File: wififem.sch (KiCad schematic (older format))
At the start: 36 parts, among them J1 Conn_Coaxial, J2 Conn_Coaxial, J3 Conn_Coaxial, J4 Conn_Coaxial, U1 MCP6566, U2 74HCT04, U3 SE2611T

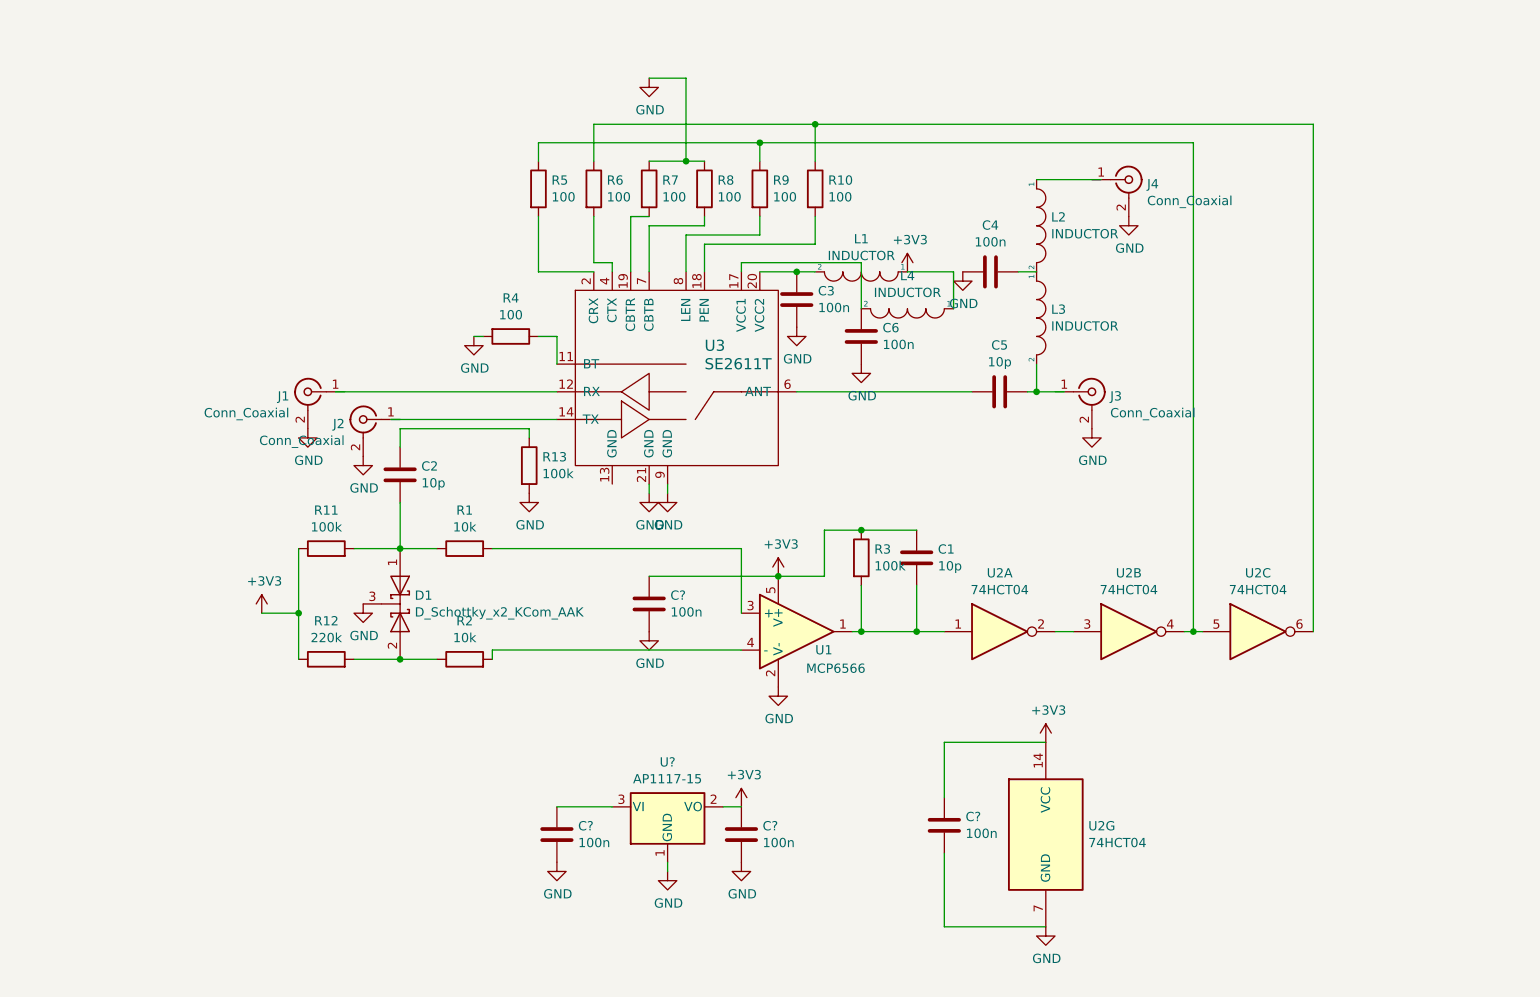
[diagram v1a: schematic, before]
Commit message: Replaced directional coupler with simple parallel connection. Layout almost done
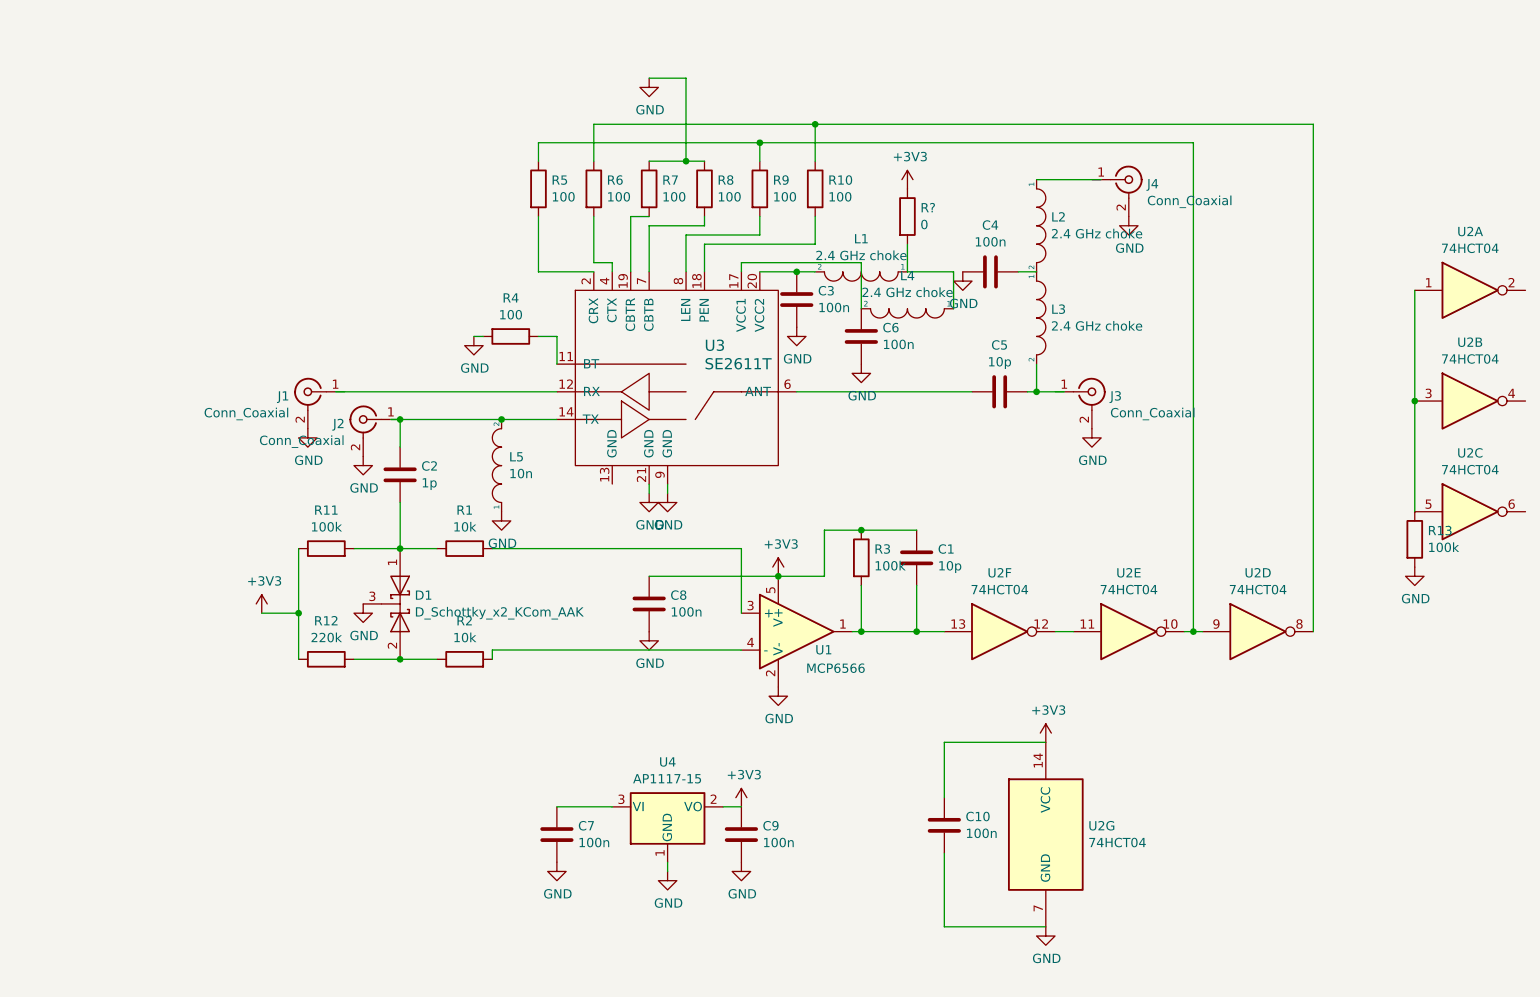
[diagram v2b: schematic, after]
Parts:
- added L5: 10n, Inductors_SMD:L_0805_HandSoldering, symbol pspice:INDUCTOR
- added R?: 0, Resistors_SMD:R_0805_HandSoldering, symbol device:R
- added unit 4 of U2
- added unit 5 of U2
- added unit 6 of U2
- C2: value 10p -> 1p
- L1, L2, L3, L4: value INDUCTOR -> 2.4 GHz choke
- gave numbers to parts that had none: 5
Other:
- moved on the sheet: U2A, U2B, U2C
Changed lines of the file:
@@
 L Logic_74xx:74HCT04 U2
 U 1 1 5A159D7B
-P 7400 3950
-F 0 "U2" H 7400 4267 50  0000 C CNN
-F 1 "74HCT04" H 7400 4176 50  0000 C CNN
-F 2 "Housings_SOIC:SOIC-14_3.9x8.7mm_Pitch1.27mm" H 7400 3950 50  0001 C CNN
-F 3 "http://www.nxp.com/documents/data_sheet/74HC_HCT04.pdf" H 7400 3950 50  0001 C CNN
-	1    7400 3950
+P 9950 2100
+F 0 "U2" H 9950 2417 50  0000 C CNN
+F 1 "74HCT04" H 9950 2326 50  0000 C CNN
+F 2 "Housings_SOIC:SOIC-14_3.9x8.7mm_Pitch1.27mm" H 9950 2100 50  0001 C CNN
+F 3 "http://www.nxp.com/documents/data_sheet/74HC_HCT04.pdf" H 9950 2100 50  0001 C CNN
+	1    9950 2100
 	1    0    0    -1
 $EndComp
@@
 L Logic_74xx:74HCT04 U2
 U 2 1 5A159F5E
-P 8100 3950
-F 0 "U2" H 8100 4267 50  0000 C CNN
-F 1 "74HCT04" H 8100 4176 50  0000 C CNN
-F 2 "" H 8100 3950 50  0001 C CNN
-F 3 "http://www.nxp.com/documents/data_sheet/74HC_HCT04.pdf" H 8100 3950 50  0001 C CNN
-	2    8100 3950
-	1    0    0    -1
-$EndComp
-$Comp
-L Logic_74xx:74HCT04 U2
-U 3 1 5A15A004
-P 8800 3950
-F 0 "U2" H 8800 4267 50  0000 C CNN
-F 1 "74HCT04" H 8800 4176 50  0000 C CNN
-F 2 "" H 8800 3950 50  0001 C CNN
-F 3 "http://www.nxp.com/documents/data_sheet/74HC_HCT04.pdf" H 8800 3950 50  0001 C CNN
-	3    8800 3950
+P 9950 2700
+F 0 "U2" H 9950 3017 50  0000 C CNN
+F 1 "74HCT04" H 9950 2926 50  0000 C CNN
+F 2 "" H 9950 2700 50  0001 C CNN
+F 3 "http://www.nxp.com/documents/data_sheet/74HC_HCT04.pdf" H 9950 2700 50  0001 C CNN
+	2    9950 2700
 	1    0    0    -1
 $EndComp
@@
 P 7600 2250
 F 0 "L3" V 7554 2328 50  0000 L CNN
-F 1 "INDUCTOR" V 7645 2328 50  0000 L CNN
+F 1 "2.4 GHz choke" V 7645 2328 50  0000 L CNN
 F 2 "Inductors_SMD:L_0805_HandSoldering" H 7600 2250 50  0001 C CNN
 F 3 "" H 7600 2250 50  0001 C CNN
@@
 P 4150 3100
 F 0 "C2" H 4035 3054 50  0000 R CNN
-F 1 "10p" H 4035 3145 50  0000 R CNN
+F 1 "1p" H 4035 3145 50  0000 R CNN
 F 2 "Capacitors_SMD:C_0805_HandSoldering" H 4188 2950 50  0001 C CNN
 F 3 "" H 4150 3100 50  0001 C CNN
@@
 P 7600 1750
 F 0 "L2" V 7554 1828 50  0000 L CNN
-F 1 "INDUCTOR" V 7645 1828 50  0000 L CNN
+F 1 "2.4 GHz choke" V 7645 1828 50  0000 L CNN
 F 2 "Inductors_SMD:L_0805_HandSoldering" H 7600 1750 50  0001 C CNN
 F 3 "" H 7600 1750 50  0001 C CNN
@@
 P 6650 2000
 F 0 "L1" H 6650 1822 50  0000 C CNN
-F 1 "INDUCTOR" H 6650 1913 50  0000 C CNN
+F 1 "2.4 GHz choke" H 6650 1913 50  0000 C CNN
 F 2 "Inductors_SMD:L_0805_HandSoldering" H 6650 2000 50  0001 C CNN
 F 3 "" H 6650 2000 50  0001 C CNN
@@
 L power:+3V3 #PWR015
 U 1 1 5A17CF72
-P 6900 2000
-F 0 "#PWR015" H 6900 1850 50  0001 C CNN
-F 1 "+3V3" H 6915 2173 50  0000 C CNN
-F 2 "" H 6900 2000 50  0001 C CNN
-F 3 "" H 6900 2000 50  0001 C CNN
-	1    6900 2000
+P 6900 1550
+F 0 "#PWR015" H 6900 1400 50  0001 C CNN
+F 1 "+3V3" H 6915 1723 50  0000 C CNN
+F 2 "" H 6900 1550 50  0001 C CNN
+F 3 "" H 6900 1550 50  0001 C CNN
+	1    6900 1550
 	1    0    0    -1
 $EndComp
@@
 P 6900 2200
 F 0 "L4" H 6900 2022 50  0000 C CNN
-F 1 "INDUCTOR" H 6900 2113 50  0000 C CNN
+F 1 "2.4 GHz choke" H 6900 2113 50  0000 C CNN
 F 2 "Inductors_SMD:L_0805_HandSoldering" H 6900 2200 50  0001 C CNN
 F 3 "" H 6900 2200 50  0001 C CNN
@@
 	6000 1950 6000 2000
 Wire Wire Line
-	4150 2950 4150 2850
-Wire Wire Line
-	4150 2850 4850 2850
-Wire Wire Line
-	4850 2850 4850 2900
-$Comp
-L power:GND #PWR017
-U 1 1 5A18CCA2
-P 4850 3200
-F 0 "#PWR017" H 4850 2950 50  0001 C CNN
-F 1 "GND" H 4855 3027 50  0000 C CNN
-F 2 "" H 4850 3200 50  0001 C CNN
-F 3 "" H 4850 3200 50  0001 C CNN
-	1    4850 3200
-	1    0    0    -1
-$EndComp
+	4150 2800 4150 2950
 $Comp
 L device:D_Schottky_x2_KCom_AAK D1
@@
 	0    1    1    0
 $EndComp
-$Comp
-L device:R R13
-U 1 1 5A18D0FD
-P 4850 3050
-F 0 "R13" H 4920 3096 50  0000 L CNN
-F 1 "100k" H 4920 3005 50  0000 L CNN
-F 2 "Resistors_SMD:R_0805_HandSoldering" V 4780 3050 50  0001 C CNN
-F 3 "" H 4850 3050 50  0001 C CNN
-	1    4850 3050
-	1    0    0    -1
-$EndComp
 Wire Wire Line
 	4150 3250 4150 3500
@@
 Connection ~ 3600 3850
 $Comp
-L regul:AP1117-15 U?
+L regul:AP1117-15 U4
 U 1 1 5A1A47EC
 P 5600 4900
-F 0 "U?" H 5600 5142 50  0000 C CNN
+F 0 "U4" H 5600 5142 50  0000 C CNN
 F 1 "AP1117-15" H 5600 5051 50  0000 C CNN
 F 2 "TO_SOT_Packages_SMD:SOT-223-3_TabPin2" H 5600 5100 50  0001 C CNN
@@
 $EndComp
 $Comp
-L power:+3V3 #PWR?
+L power:+3V3 #PWR020
 U 1 1 5A1A48D5
 P 6000 4900
-F 0 "#PWR?" H 6000 4750 50  0001 C CNN
+F 0 "#PWR020" H 6000 4750 50  0001 C CNN
 F 1 "+3V3" H 6015 5073 50  0000 C CNN
 F 2 "" H 6000 4900 50  0001 C CNN
@@
 	6000 4900 5900 4900
 $Comp
-L power:GND #PWR?
+L power:GND #PWR021
 U 1 1 5A1A6D47
 P 5600 5250
-F 0 "#PWR?" H 5600 5000 50  0001 C CNN
+F 0 "#PWR021" H 5600 5000 50  0001 C CNN
 F 1 "GND" H 5605 5077 50  0000 C CNN
 F 2 "" H 5600 5250 50  0001 C CNN
@@
 	5600 5250 5600 5200
 $Comp
-L device:C C?
+L device:C C9
 U 1 1 5A1AA377
 P 6000 5050
-F 0 "C?" H 5885 5004 50  0000 R CNN
+F 0 "C9" H 5885 5004 50  0000 R CNN
 F 1 "100n" H 5885 5095 50  0000 R CNN
 F 2 "Capacitors_SMD:C_0805_HandSoldering" H 6038 4900 50  0001 C CNN
@@
 $EndComp
 $Comp
-L power:GND #PWR?
+L power:GND #PWR022
 U 1 1 5A1AA62D
 P 6000 5200
-F 0 "#PWR?" H 6000 4950 50  0001 C CNN
+F 0 "#PWR022" H 6000 4950 50  0001 C CNN
 F 1 "GND" H 6005 5027 50  0000 C CNN
 F 2 "" H 6000 5200 50  0001 C CNN
@@
 $EndComp
 $Comp
-L device:C C?
+L device:C C7
 U 1 1 5A1AA680
 P 5000 5050
-F 0 "C?" H 4885 5004 50  0000 R CNN
+F 0 "C7" H 4885 5004 50  0000 R CNN
 F 1 "100n" H 4885 5095 50  0000 R CNN
 F 2 "Capacitors_SMD:C_0805_HandSoldering" H 5038 4900 50  0001 C CNN
@@
 	5300 4900 5000 4900
 $Comp
-L power:GND #PWR?
+L power:GND #PWR023
 U 1 1 5A1ACCE4
 P 5000 5200
-F 0 "#PWR?" H 5000 4950 50  0001 C CNN
+F 0 "#PWR023" H 5000 4950 50  0001 C CNN
 F 1 "GND" H 5005 5027 50  0000 C CNN
 F 2 "" H 5000 5200 50  0001 C CNN
@@
 $EndComp
 $Comp
-L device:C C?
+L device:C C8
 U 1 1 5A1ACD39
 P 5500 3800
-F 0 "C?" H 5385 3754 50  0000 R CNN
+F 0 "C8" H 5385 3754 50  0000 R CNN
 F 1 "100n" H 5385 3845 50  0000 R CNN
 F 2 "Capacitors_SMD:C_0805_HandSoldering" H 5538 3650 50  0001 C CNN
@@
 Connection ~ 6200 3650
 $Comp
-L power:GND #PWR?
+L power:GND #PWR024
 U 1 1 5A1B10BA
 P 5500 3950
-F 0 "#PWR?" H 5500 3700 50  0001 C CNN
+F 0 "#PWR024" H 5500 3700 50  0001 C CNN
 F 1 "GND" H 5505 3777 50  0000 C CNN
 F 2 "" H 5500 3950 50  0001 C CNN
@@
 $EndComp
 $Comp
-L device:C C?
+L device:C C10
 U 1 1 5A1B1111
 P 7100 5000
-F 0 "C?" H 6985 4954 50  0000 R CNN
+F 0 "C10" H 6985 4954 50  0000 R CNN
 F 1 "100n" H 6985 5045 50  0000 R CNN
 F 2 "Capacitors_SMD:C_0805_HandSoldering" H 7138 4850 50  0001 C CNN
@@
 Wire Wire Line
 	7100 5550 7100 5150
+Connection ~ 4150 2800
+$Comp
+L pspice:INDUCTOR L5
+U 1 1 5A1BC783
+P 4700 3050
+F 0 "L5" V 4746 3010 50  0000 R CNN
+F 1 "10n" V 4655 3010 50  0000 R CNN
+F 2 "Inductors_SMD:L_0805_HandSoldering" H 4700 3050 50  0001 C CNN
+F 3 "" H 4700 3050 50  0001 C CNN
+	1    4700 3050
+	0    -1   -1   0
+$EndComp
+Connection ~ 4700 2800
+$Comp
+L power:GND #PWR017
+U 1 1 5A1C03BF
+P 4700 3300
+F 0 "#PWR017" H 4700 3050 50  0001 C CNN
+F 1 "GND" H 4705 3127 50  0000 C CNN
+F 2 "" H 4700 3300 50  0001 C CNN
+F 3 "" H 4700 3300 50  0001 C CNN
+	1    4700 3300
+	1    0    0    -1
+$EndComp
+$Comp
+L Logic_74xx:74HCT04 U2
+U 4 1 5A1C573B
+P 8800 3950
+F 0 "U2" H 8800 4267 50  0000 C CNN
+F 1 "74HCT04" H 8800 4176 50  0000 C CNN
+F 2 "" H 8800 3950 50  0001 C CNN
+F 3 "http://www.nxp.com/documents/data_sheet/74HC_HCT04.pdf" H 8800 3950 50  0001 C CNN
+	4    8800 3950
+	1    0    0    -1
+$EndComp
+$Comp
+L Logic_74xx:74HCT04 U2
+U 5 1 5A1C586C
+P 8100 3950
+F 0 "U2" H 8100 4267 50  0000 C CNN
+F 1 "74HCT04" H 8100 4176 50  0000 C CNN
+F 2 "" H 8100 3950 50  0001 C CNN
+F 3 "http://www.nxp.com/documents/data_sheet/74HC_HCT04.pdf" H 8100 3950 50  0001 C CNN
+	5    8100 3950
+	1    0    0    -1
+$EndComp
+$Comp
+L Logic_74xx:74HCT04 U2
+U 6 1 5A1C59B9
+P 7400 3950
+F 0 "U2" H 7400 4267 50  0000 C CNN
+F 1 "74HCT04" H 7400 4176 50  0000 C CNN
+F 2 "" H 7400 3950 50  0001 C CNN
+F 3 "http://www.nxp.com/documents/data_sheet/74HC_HCT04.pdf" H 7400 3950 50  0001 C CNN
+	6    7400 3950
+	1    0    0    -1
+$EndComp
+$Comp
+L Logic_74xx:74HCT04 U2
+U 3 1 5A15A004
+P 9950 3300
+F 0 "U2" H 9950 3617 50  0000 C CNN
+F 1 "74HCT04" H 9950 3526 50  0000 C CNN
+F 2 "" H 9950 3300 50  0001 C CNN
+F 3 "http://www.nxp.com/documents/data_sheet/74HC_HCT04.pdf" H 9950 3300 50  0001 C CNN
+	3    9950 3300
+	1    0    0    -1
+$EndComp
+Wire Wire Line
+	9650 2100 9650 3300
+Connection ~ 9650 2700
+$Comp
+L power:GND #PWR025
+U 1 1 5A1CD3BC
+P 9650 3600
+F 0 "#PWR025" H 9650 3350 50  0001 C CNN
+F 1 "GND" H 9655 3427 50  0000 C CNN
+F 2 "" H 9650 3600 50  0001 C CNN
+F 3 "" H 9650 3600 50  0001 C CNN
+	1    9650 3600
+	1    0    0    -1
+$EndComp
+$Comp
+L device:R R13
+U 1 1 5A1D64EB
+P 9650 3450
+F 0 "R13" H 9720 3496 50  0000 L CNN
+F 1 "100k" H 9720 3405 50  0000 L CNN
+F 2 "Resistors_SMD:R_0805_HandSoldering" V 9580 3450 50  0001 C CNN
+F 3 "" H 9650 3450 50  0001 C CNN
+	1    9650 3450
+	1    0    0    -1
+$EndComp
+$Comp
+L device:R R?
+U 1 1 5A1DB8B4
+P 6900 1700
+F 0 "R?" H 6970 1746 50  0000 L CNN
+F 1 "0" H 6970 1655 50  0000 L CNN
+F 2 "Resistors_SMD:R_0805_HandSoldering" V 6830 1700 50  0001 C CNN
+F 3 "" H 6900 1700 50  0001 C CNN
+	1    6900 1700
+	1    0    0    -1
+$EndComp
+Wire Wire Line
+	6900 1850 6900 2000
 $EndSCHEMATC

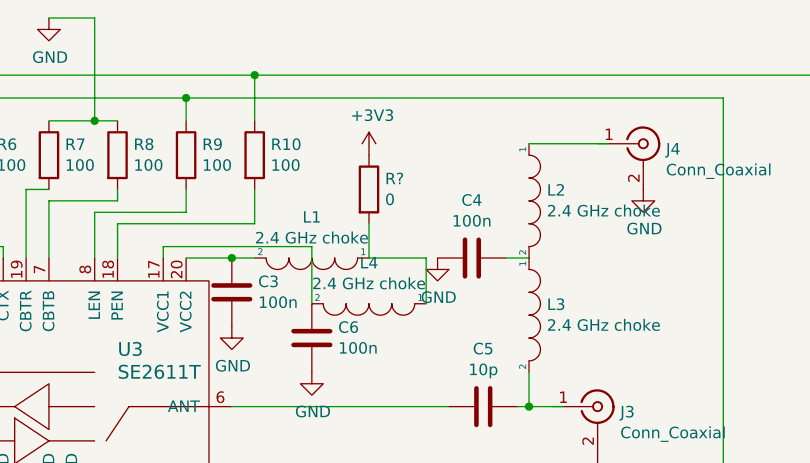
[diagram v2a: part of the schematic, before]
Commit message: RF layout improvement
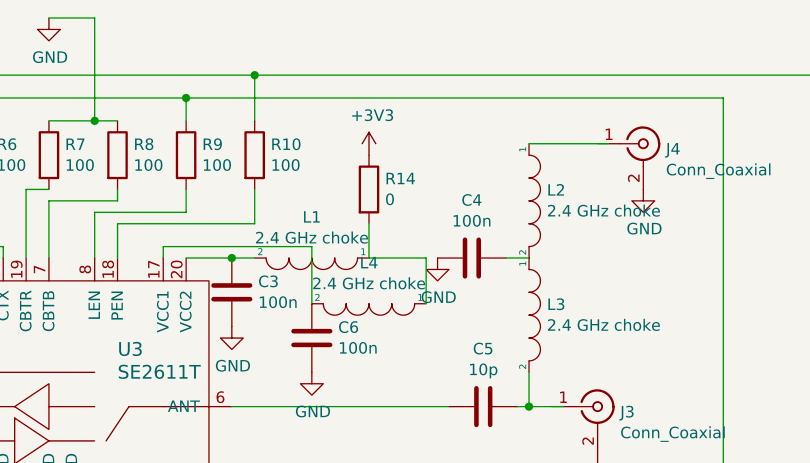
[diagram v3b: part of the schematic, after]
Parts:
- gave numbers to parts that had none: 1
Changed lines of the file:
@@
 $EndComp
 $Comp
-L device:R R?
+L device:R R14
 U 1 1 5A1DB8B4
 P 6900 1700
-F 0 "R?" H 6970 1746 50  0000 L CNN
+F 0 "R14" H 6970 1746 50  0000 L CNN
 F 1 "0" H 6970 1655 50  0000 L CNN
 F 2 "Resistors_SMD:R_0805_HandSoldering" V 6830 1700 50  0001 C CNN

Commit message: Everything in layout, DRC passes
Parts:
- removed J4: Conn_Coaxial, Connectors:SMA_THT_Jack_Straight, symbol Connector:Conn_Coaxial
- added D2: DIODE, Resistors_SMD:R_0805_HandSoldering, symbol pspice:DIODE
- added J4: Conn_01x05, Socket_Strips:Socket_Strip_Straight_1x05_Pitch2.54mm, symbol Connector:Conn_01x05
- added L6: ferrite bead, Inductors_SMD:L_0805_HandSoldering, symbol pspice:INDUCTOR
- added MK1, MK2, MK3, MK4: Mounting_Hole_PAD, Mounting_Holes:MountingHole_3.2mm_M3_Pad, symbol Mechanical:Mounting_Hole_PAD
- L1, L2, L4: value 2.4 GHz choke -> ferrite bead
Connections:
- wire segments 72 -> 84
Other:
- moved on the sheet: C4, L2

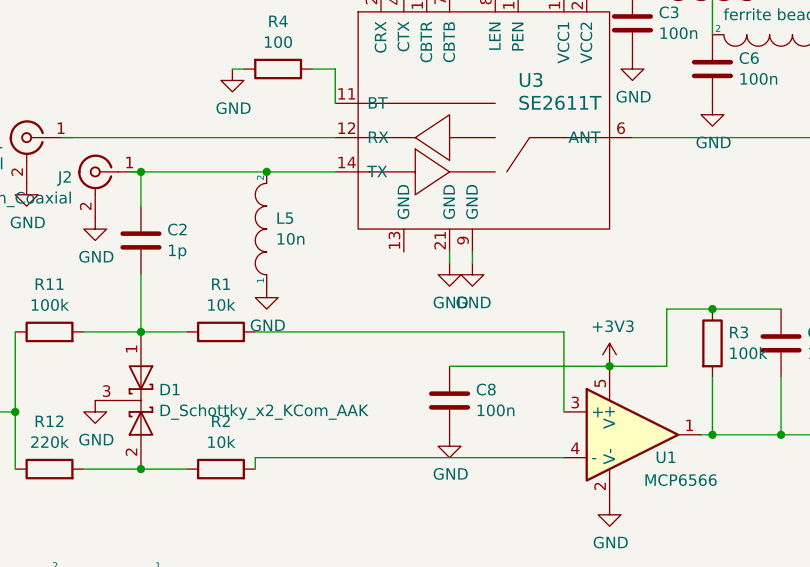
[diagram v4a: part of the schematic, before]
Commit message: Added missing ground pin in FEM
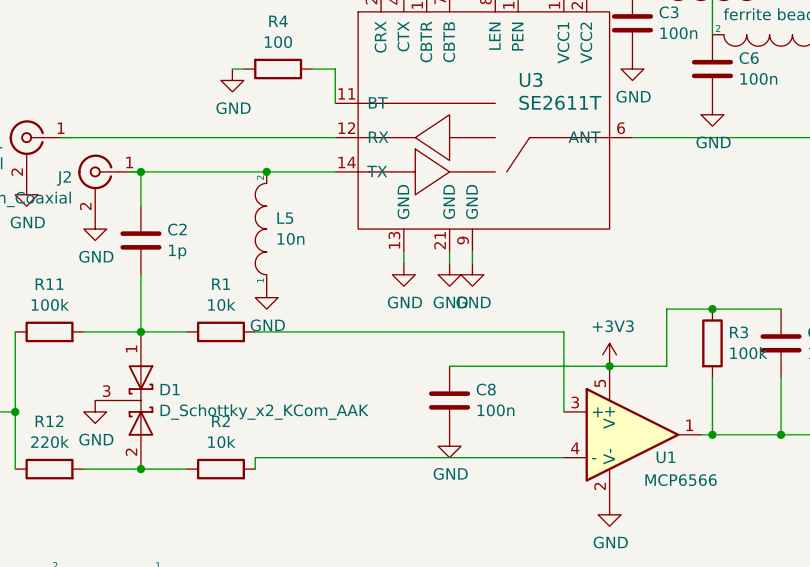
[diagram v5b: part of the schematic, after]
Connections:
- wire segments 84 -> 85
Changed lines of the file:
@@
 	7600 2000 7600 1950
 Connection ~ 7600 1950
+$Comp
+L power:GND #PWR?
+U 1 1 5A15FD74
+P 5300 3200
+F 0 "#PWR?" H 5300 2950 50  0001 C CNN
+F 1 "GND" H 5305 3027 50  0000 C CNN
+F 2 "" H 5300 3200 50  0001 C CNN
+F 3 "" H 5300 3200 50  0001 C CNN
+	1    5300 3200
+	1    0    0    -1
+$EndComp
+Wire Wire Line
+	5300 3200 5300 3150
 $EndSCHEMATC
